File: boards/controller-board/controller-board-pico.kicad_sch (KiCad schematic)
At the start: 53 parts, among them J1 Phoenix 1935161, J2 Conn_01x02, J3 Conn_01x02, J4 Conn_01x02, J5 Conn_01x03, J6 Phoenix 1995499, J7 Conn_01x03, J8 Conn_01x03, Q1 PMV45EN, Q2 Goford_G11S_20V_11A, U2 ADS1015IRUGR, U4 RPi_Pico, U5 MCP4728

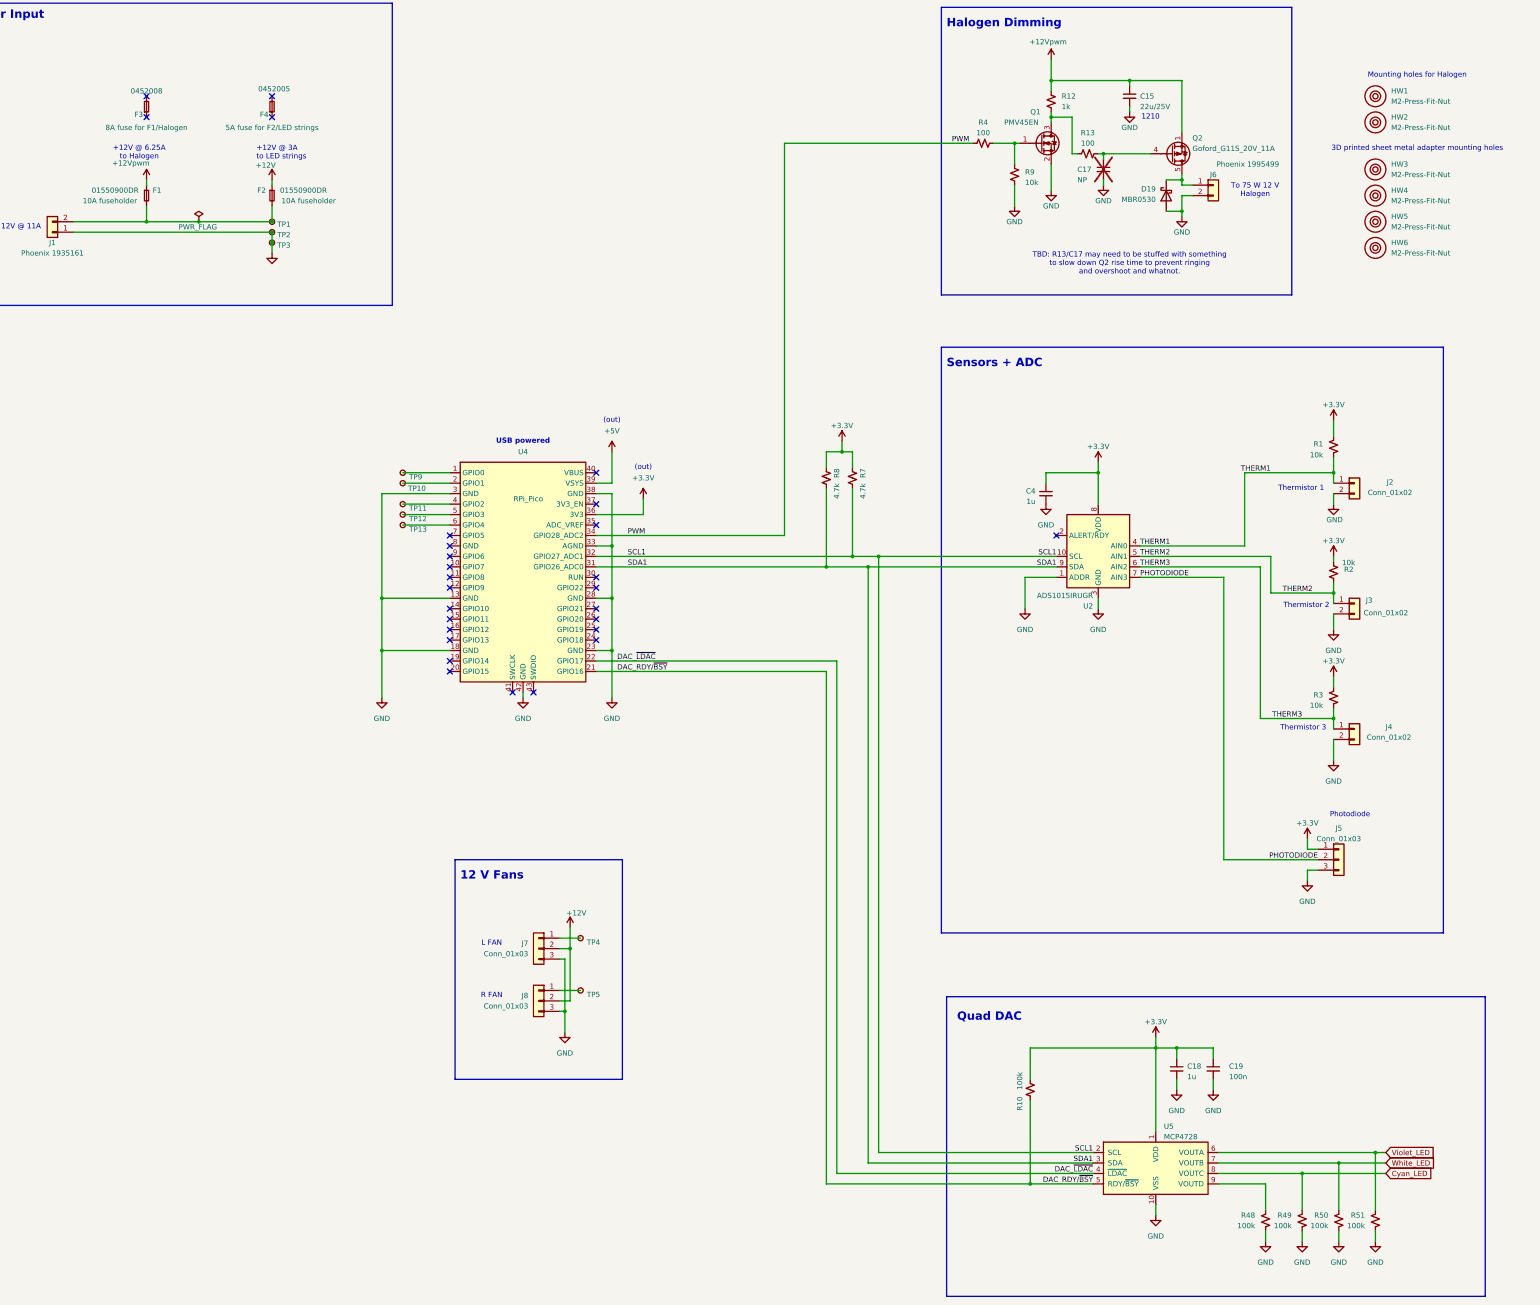
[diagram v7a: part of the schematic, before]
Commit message: Updated 3D models, ground stitching, zone layout, lots of polishing and checking before fab.
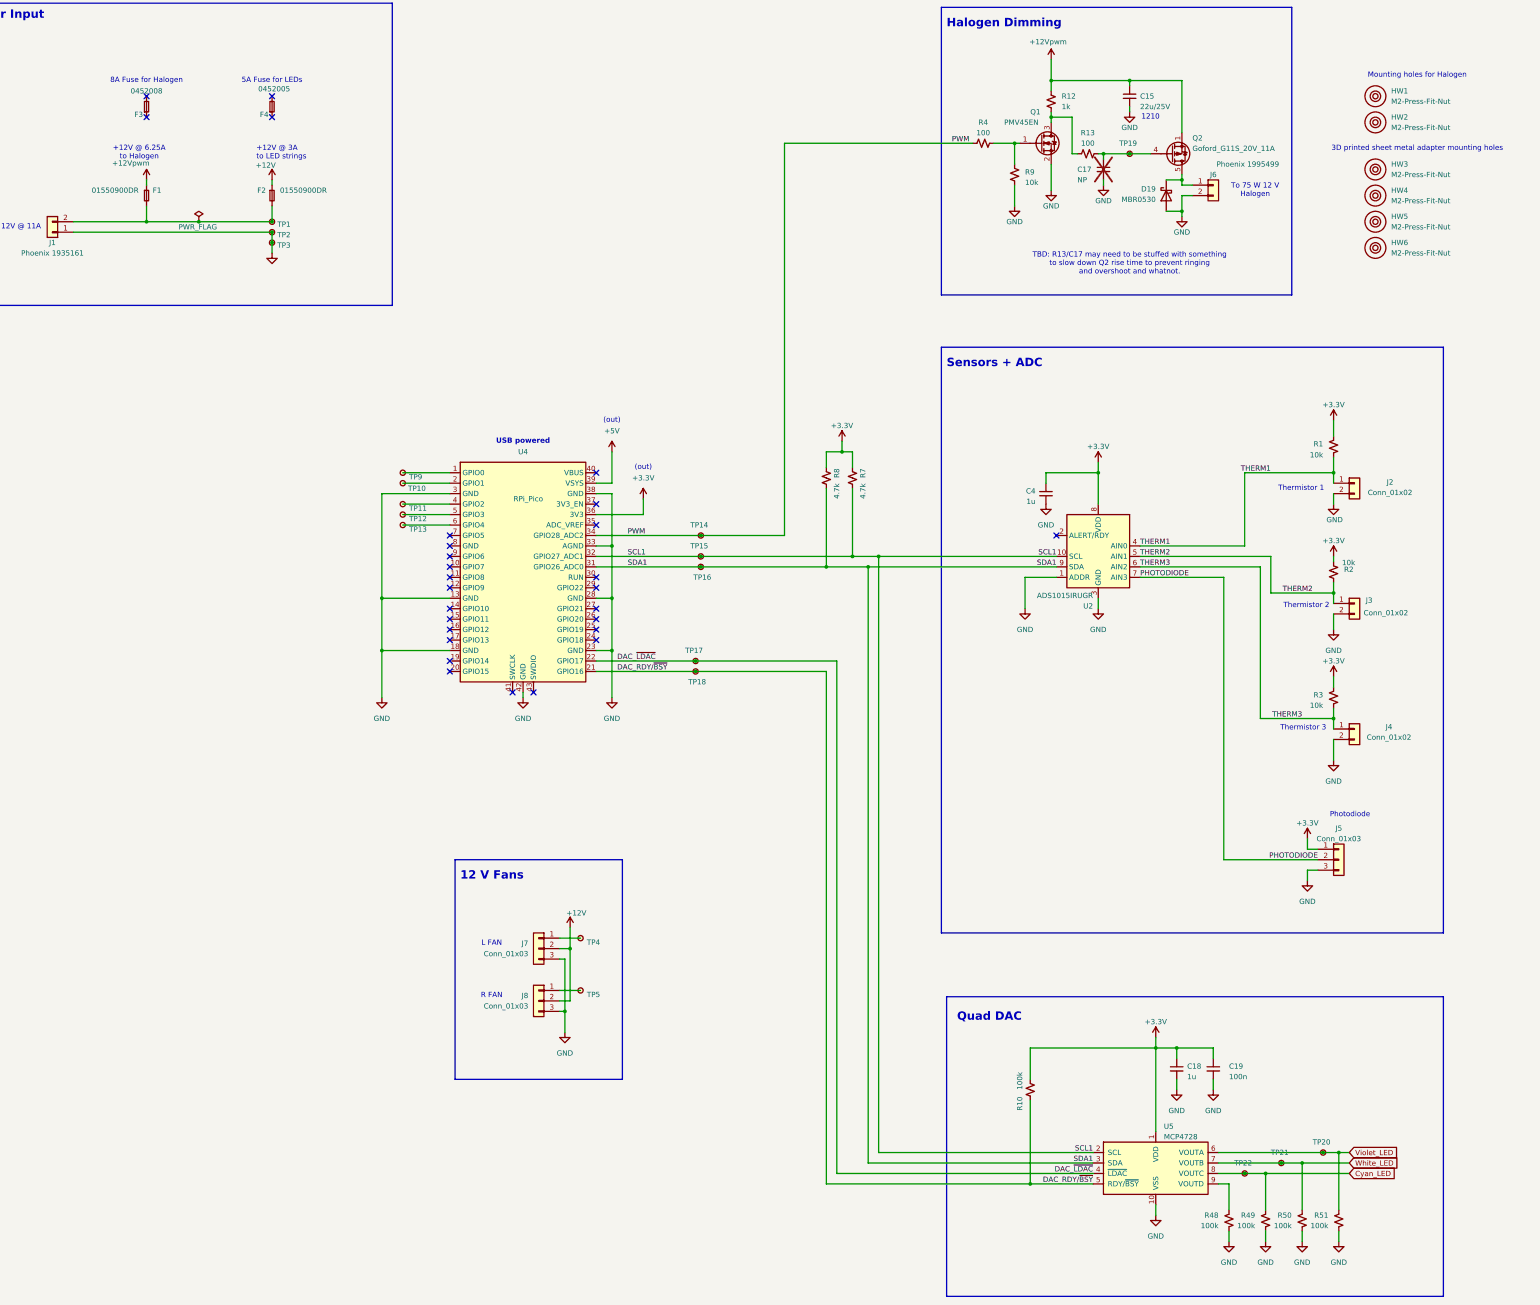
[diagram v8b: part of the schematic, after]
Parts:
- added TP14, TP15, TP16, TP17, TP18, TP19, TP20, TP21, TP22: TestPoint-MinTH, oresat-misc:TestPoint-MinTH, symbol oresat-misc:TestPoint-MinTH
- D19: DPN (none) -> MBR0530CT-ND; Distributor (none) -> DigiKey; MFR (none) -> onsemi; MPN (none) -> MBR0530
- HW1, HW2, HW3, HW4, HW5, HW6: now left out of the parts list
- J2, J3, J4: DPN (none) -> 861400021YO2LF-ND; MFR (none) -> Amphenol ICC (FCI); MPN (none) -> 861400021YO2LF
- J5: DPN (none) -> 609-861400031YO2LF-ND; MFR (none) -> Amphenol ICC (FCI); MPN (none) -> 861400031YO2LF
- J7, J8: DPN (none) -> 609-861400031YO2LF-ND; Distributor (none) -> DigiKey; MFR (none) -> Amphenol ICC (FCI); MPN (none) -> 861400031YO2LF
- TP1, TP10, TP11, TP12, TP13, TP2, TP3, TP4, TP5, TP9: Distributor DigiKey -> (none); now left out of the parts list
- U5: Distributor (none) -> DigiKey
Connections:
- net Cyan_LED: now also TP22.1
- net DAC_RDY/~{BSY}: now also TP18.1
- net DAC_~{LDAC}: now also TP17.1
- net PWM: now also TP14.1
- net SCL1: now also TP15.1
- net SDA1: now also TP16.1
- net Violet_LED: now also TP20.1
- net White_LED: now also TP21.1
- net at C17.1, Q2.4 (G), R13.2: now also TP19.1
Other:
- note added: "5A Fuse for LEDs"
- note added: "8A Fuse for Halogen"
- moved on the sheet: R48, R49, R50, R51
